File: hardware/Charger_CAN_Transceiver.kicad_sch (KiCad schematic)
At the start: 9 parts, among them IC2 TCAN3413DR

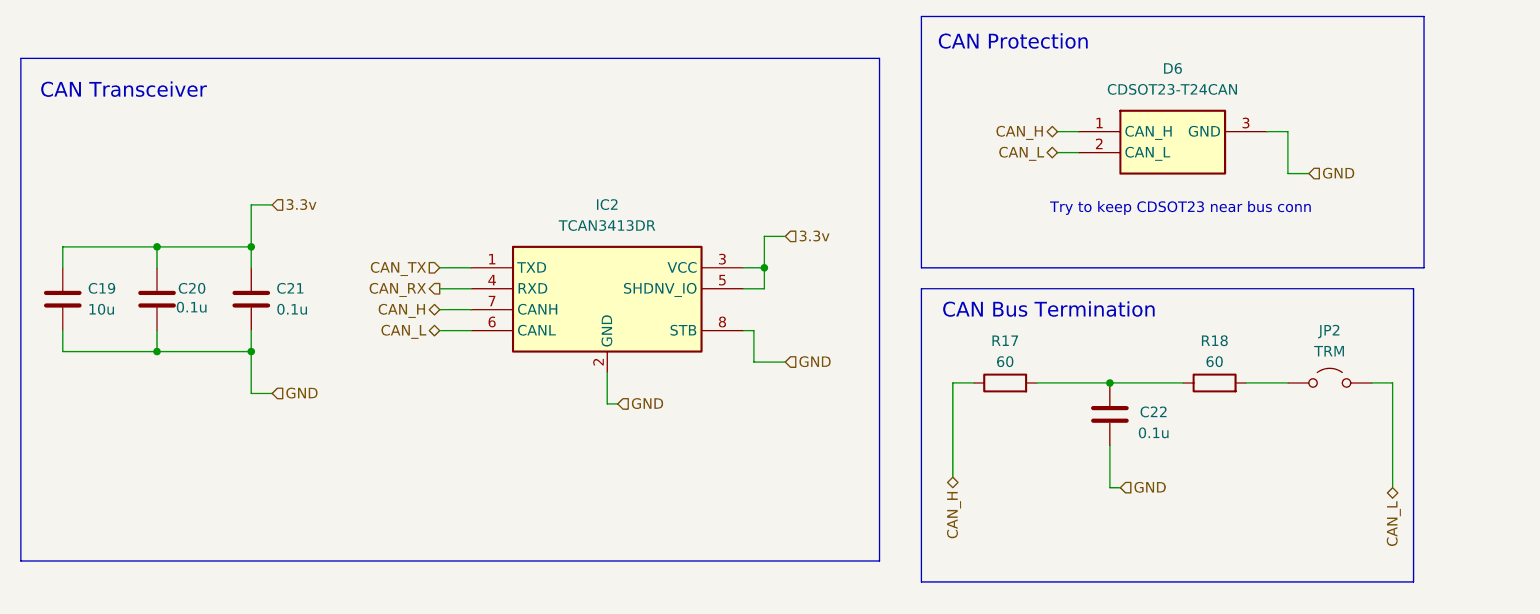
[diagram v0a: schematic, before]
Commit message: finished schematic except for 12v buck boost
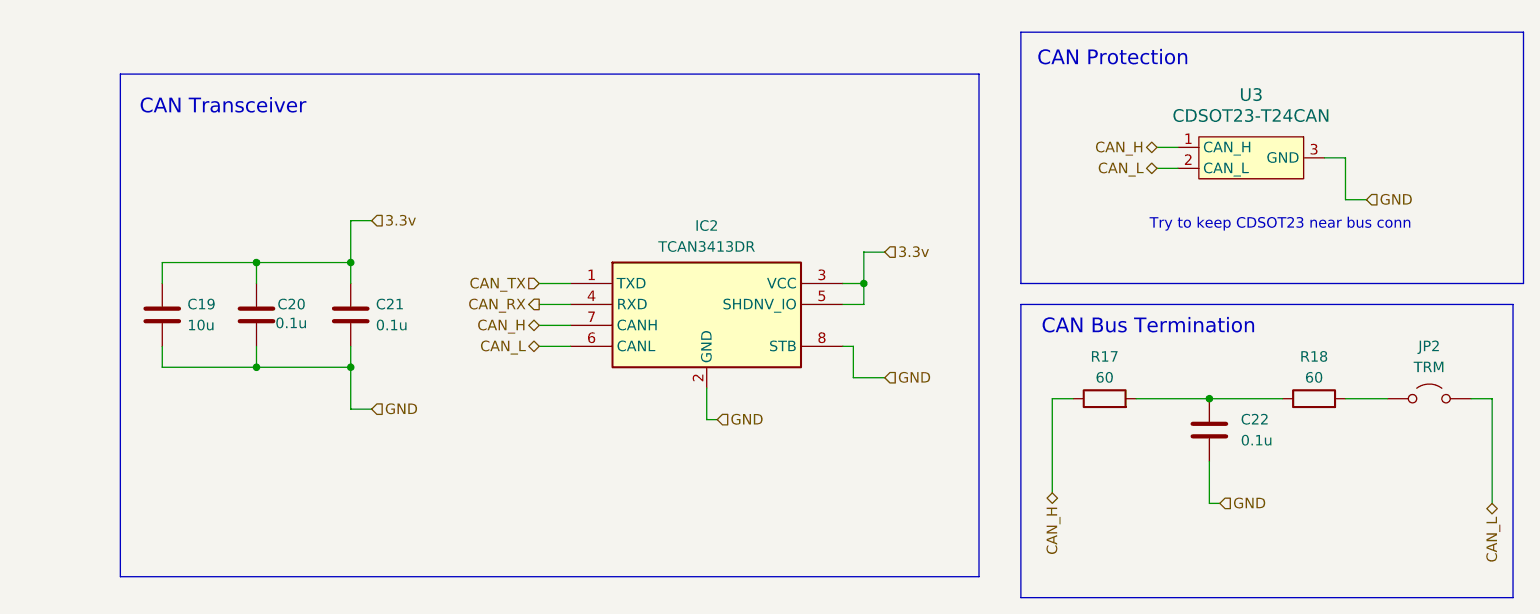
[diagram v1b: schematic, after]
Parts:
- removed C22: 0.1u, Capacitor_SMD:C_0603_1608Metric_Pad1.08x0.95mm_HandSolder, symbol ECE319K:C
- removed D6: CDSOT23-T24CAN, LHRS_Passives:CDSOT23-T24CAN, symbol CDSOT23-T24CAN:CDSOT23-T24CAN
- removed IC2: TCAN3413DR, LHRS_Passives:TCAN3413DR, symbol TCAN3413DR:TCAN3413DR
- added C22: 0.1u, symbol Device:C
- added IC2: TCAN3413DR, LHRS_Passives:TCAN3413DR, symbol lhrs_ics:TCAN3413DR
- added U3: CDSOT23-T24CAN, LHRS_ICs:CDSOT23-T24CAN, symbol lhrs_ics:CDSOT23-T24CAN
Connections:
- net 3.3v: now also IC2.3 (VCC), IC2.5 (SHDNV_IO)
- net CAN_H: now also IC2.7 (CANH), U3.1 (CAN_H)
- net CAN_L: now also IC2.6 (CANL), U3.2 (CAN_L)
- net CAN_RX: now also IC2.4 (RXD)
- net CAN_TX: now also IC2.1 (TXD)
- net GND: now also C22.2, IC2.2 (GND), IC2.8 (STB), U3.3 (GND)
- net at R17.2, R18.1: now also C22.1

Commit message: added 12V buck boost
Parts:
- C23: renamed from C22; footprint (none) -> Capacitor_SMD:C_0603_1608Metric_Pad1.08x0.95mm_HandSolder
- renumbered C19 to C20, C20 to C21, C21 to C22, R17 to R21, R18 to R22
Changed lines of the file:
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@@
 		(in_pos_files yes)
 		(dnp no)
-		(property "Reference" "C20"
+		(property "Reference" "C21"
 			(at 88.265 75.565 0)
 			(show_name no)
@@
 			(project "PS-BPSLeader"
 				(path "/d4a4ed4f-0983-4aef-b212-0e3284ab3963/5da56964-fa04-4fec-bdfe-c6acfeda5c9a/b53616f8-f3a9-4a42-a33c-3ef3f96bd2e0"
-					(reference "C20")
+					(reference "C21")
 					(unit 1)
 				)
@@
 		(in_pos_files yes)
 		(dnp no)
-		(property "Reference" "R17"
+		(property "Reference" "R21"
 			(at 188.595 81.915 90)
 			(show_name no)
@@
 			(project "PS-BPSLeader"
 				(path "/d4a4ed4f-0983-4aef-b212-0e3284ab3963/5da56964-fa04-4fec-bdfe-c6acfeda5c9a/b53616f8-f3a9-4a42-a33c-3ef3f96bd2e0"
-					(reference "R17")
+					(reference "R21")
 					(unit 1)
 				)
@@
 		(in_pos_files yes)
 		(dnp no)
-		(property "Reference" "C21"
+		(property "Reference" "C22"
 			(at 100.203 75.565 0)
 			(show_name no)
@@
 			(project "PS-BPSLeader"
 				(path "/d4a4ed4f-0983-4aef-b212-0e3284ab3963/5da56964-fa04-4fec-bdfe-c6acfeda5c9a/b53616f8-f3a9-4a42-a33c-3ef3f96bd2e0"
-					(reference "C21")
+					(reference "C22")
 					(unit 1)
 				)
@@
 		(in_pos_files yes)
 		(dnp no)
-		(property "Reference" "C19"
+		(property "Reference" "C20"
 			(at 77.343 75.565 0)
 			(show_name no)
@@
 			(project "PS-BPSLeader"
 				(path "/d4a4ed4f-0983-4aef-b212-0e3284ab3963/5da56964-fa04-4fec-bdfe-c6acfeda5c9a/b53616f8-f3a9-4a42-a33c-3ef3f96bd2e0"
-					(reference "C19")
+					(reference "C20")
 					(unit 1)
 				)
@@
 		(dnp no)
 		(fields_autoplaced yes)
-		(property "Reference" "C22"
+		(property "Reference" "C23"
 			(at 205.105 89.5349 0)
 			(show_name no)
@@
 			)
 		)
-		(property "Footprint" ""
+		(property "Footprint" "Capacitor_SMD:C_0603_1608Metric_Pad1.08x0.95mm_HandSolder"
 			(at 202.2602 94.615 0)
 			(hide yes)
@@
 			(project "PS-BPSLeader"
 				(path "/d4a4ed4f-0983-4aef-b212-0e3284ab3963/5da56964-fa04-4fec-bdfe-c6acfeda5c9a/b53616f8-f3a9-4a42-a33c-3ef3f96bd2e0"
-					(reference "C22")
+					(reference "C23")
 					(unit 1)
 				)
@@
 		(in_pos_files yes)
 		(dnp no)
-		(property "Reference" "R18"
+		(property "Reference" "R22"
 			(at 213.995 81.915 90)
 			(show_name no)
@@
 			(project "PS-BPSLeader"
 				(path "/d4a4ed4f-0983-4aef-b212-0e3284ab3963/5da56964-fa04-4fec-bdfe-c6acfeda5c9a/b53616f8-f3a9-4a42-a33c-3ef3f96bd2e0"
-					(reference "R18")
-					(unit 1)
-				)
+					(reference "R22")
+					(unit 1)
+				)
